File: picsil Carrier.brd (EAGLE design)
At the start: 95 x 54.3 mm, 52 parts, among them IC1 NAND, J1 STX-3120-3BM, J2 STX-3120-3BM, J3 STX-3120-3BM, J5 S2B-PH-SM4-TB(LF)(SN), J6 47346-1001, Q1 MMBT2222A, U1 MB85RC256VPF-G-JNERE2, U11 BORON, U2 TPL5010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

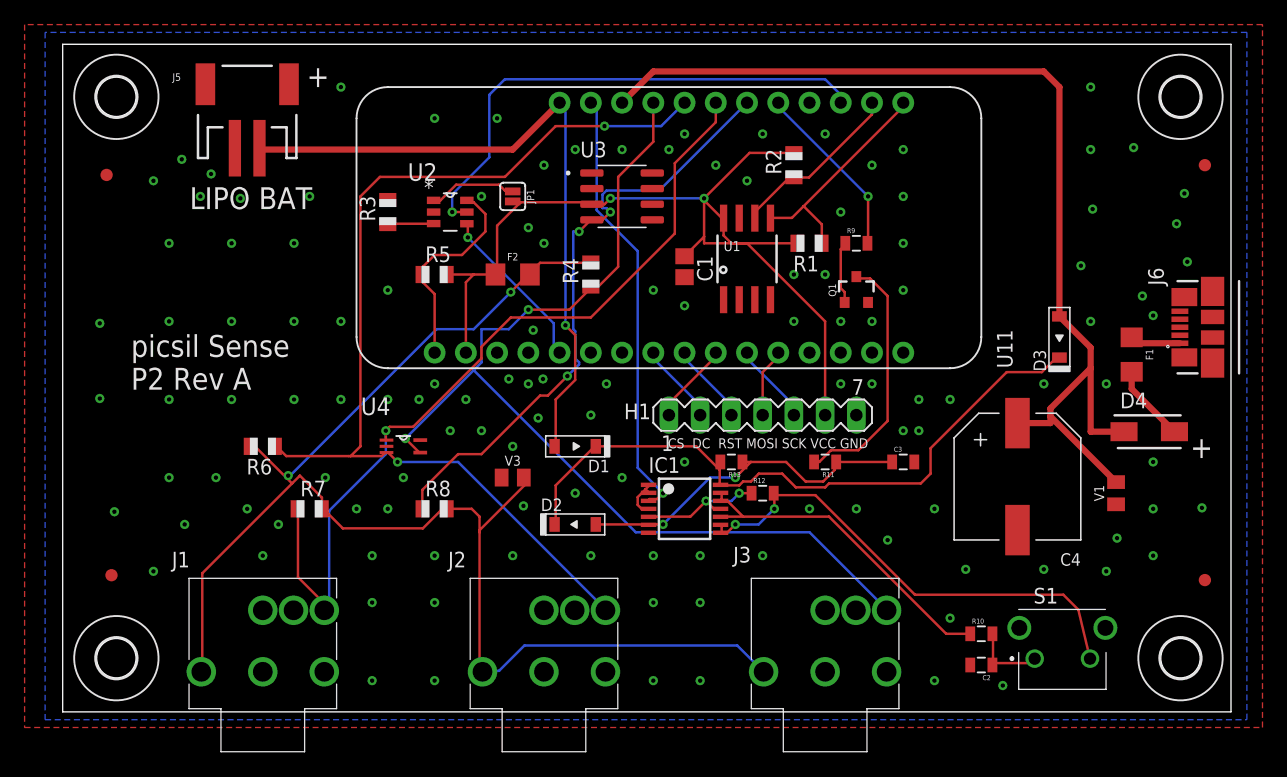
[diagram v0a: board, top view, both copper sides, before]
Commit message: rerouted VCC to U1
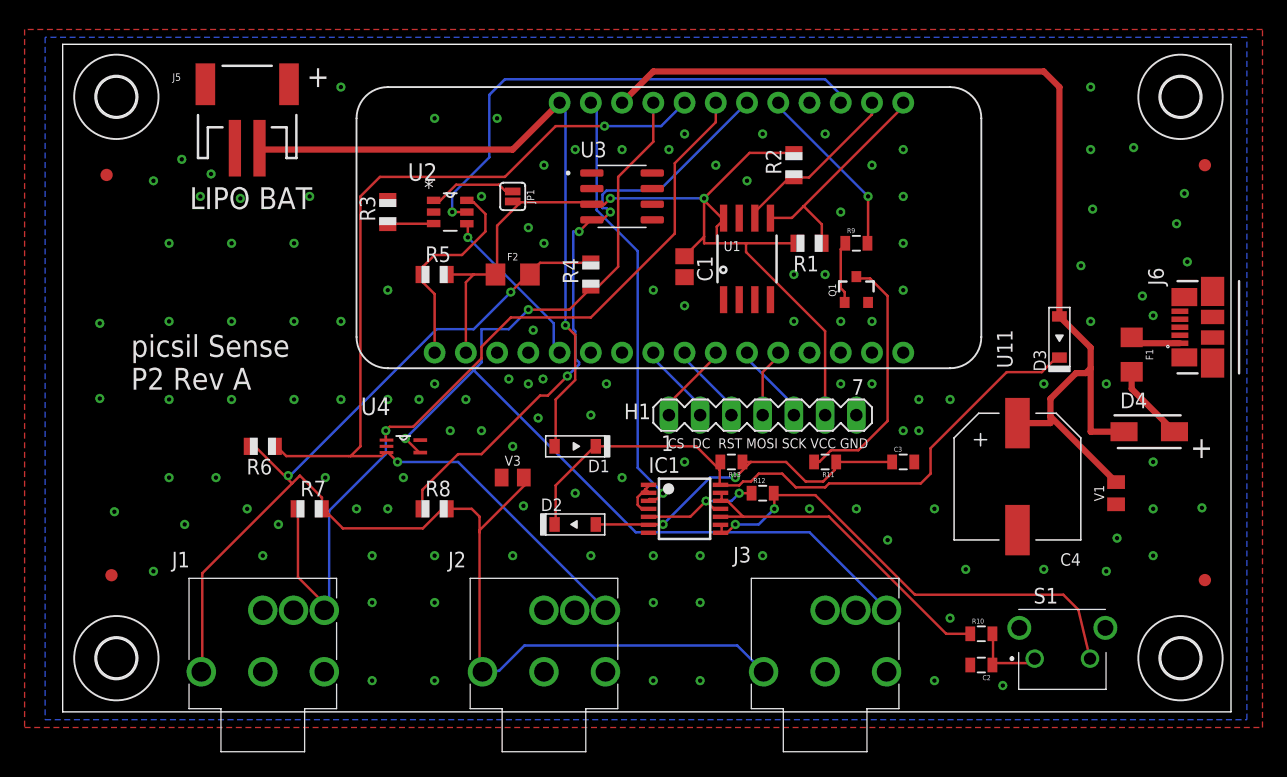
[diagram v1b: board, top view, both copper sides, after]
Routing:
- net VCC: track 78.1 -> 76.9 mm
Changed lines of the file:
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@@
 <vertex x="-5.000625" y="-0.635"/>
 <vertex x="92.71" y="-0.635"/>
-<vertex x="92.71" y="55.245"/>
-<vertex x="-5.000625" y="55.245"/>
+<vertex x="92.71" y="54.848125"/>
+<vertex x="-5.000625" y="54.848125"/>
 </polygon>
 <polygon width="0.1524" layer="1" isolate="0.3048">
 <vertex x="-6.6675" y="-1.27"/>
 <vertex x="93.98" y="-1.27"/>
-<vertex x="93.98" y="55.88"/>
-<vertex x="-6.6675" y="55.88"/>
+<vertex x="93.98" y="55.483125"/>
+<vertex x="-6.6675" y="55.483125"/>
 </polygon>
 <via x="52.07" y="43.18" extent="1-16" drill="0.35"/>
@@
 <wire x1="48.5775" y1="38.1" x2="48.5775" y2="38.6325" width="0.2032" layer="1"/>
 <wire x1="48.5775" y1="38.6325" x2="48.5775" y2="41.75125" width="0.2032" layer="1"/>
-<wire x1="48.5775" y1="38.1" x2="56.15" y2="38.1" width="0.2032" layer="1"/>
+<wire x1="48.5775" y1="38.1" x2="49.609375" y2="38.1" width="0.2032" layer="1"/>
+<wire x1="56.15" y1="38.1" x2="51.990625" y2="38.1" width="0.2032" layer="1"/>
+<wire x1="51.990625" y1="38.1" x2="49.609375" y2="38.1" width="0.2032" layer="1"/>
 <wire x1="31.62" y1="35.56" x2="29.845" y2="35.56" width="0.2032" layer="1"/>
 <wire x1="29.845" y1="35.56" x2="27.67" y2="35.56" width="0.2032" layer="1"/>
@@
 <wire x1="40.48125" y1="41.275" x2="40.9575" y2="41.75125" width="0.2032" layer="1"/>
 <wire x1="39.455" y1="41.275" x2="40.48125" y2="41.275" width="0.2032" layer="1"/>
-<wire x1="58.42" y1="31.75" x2="58.42" y2="24.13" width="0.2032" layer="1"/>
-<wire x1="52.07" y1="38.1" x2="58.42" y2="31.75" width="0.2032" layer="1"/>
-<wire x1="50.8" y1="38.1" x2="52.07" y2="38.1" width="0.2032" layer="1"/>
-<wire x1="50.165" y1="38.735" x2="50.8" y2="38.1" width="0.2032" layer="1"/>
-<wire x1="50.165" y1="40.005" x2="50.165" y2="38.735" width="0.2032" layer="1"/>
-<wire x1="50.165" y1="40.005" x2="50.165" y2="40.145" width="0.2032" layer="1"/>
+<wire x1="58.42" y1="24.13" x2="58.42" y2="30.95625" width="0.2032" layer="1"/>
 <via x="48.5775" y="41.75125" extent="1-16" drill="0.35"/>
 <via x="40.9575" y="41.75125" extent="1-16" drill="0.35"/>
@@
 <wire x1="29.21" y1="34.925" x2="29.845" y2="35.56" width="0.2032" layer="1"/>
 <wire x1="29.21" y1="29.21" x2="29.21" y2="34.925" width="0.2032" layer="1"/>
+<wire x1="49.609375" y1="39.449375" x2="50.165" y2="40.005" width="0.2032" layer="1"/>
+<wire x1="49.609375" y1="38.1" x2="49.609375" y2="39.449375" width="0.2032" layer="1"/>
+<wire x1="51.990625" y1="37.385625" x2="51.990625" y2="38.1" width="0.2032" layer="1"/>
+<wire x1="58.42" y1="30.95625" x2="51.990625" y2="37.385625" width="0.2032" layer="1"/>
+<wire x1="50.165" y1="40.145" x2="50.165" y2="40.005" width="0.2032" layer="1"/>
 </signal>
 <signal name="SDA">
@@
 <wire x1="80.01" y1="29.615" x2="80.01" y2="27.94" width="0.508" layer="1"/>
 <wire x1="80.01" y1="27.94" x2="80.01" y2="22.780625" width="0.508" layer="1"/>
-<wire x1="76.74" y1="24.67" x2="80.01" y2="27.94" width="0.508" layer="1"/>
+<wire x1="78.819375" y1="27.543125" x2="76.74" y2="25.46375" width="0.508" layer="1"/>
+<wire x1="78.819375" y1="27.543125" x2="79.613125" y2="27.543125" width="0.508" layer="1"/>
+<wire x1="79.613125" y1="27.543125" x2="80.01" y2="27.94" width="0.508" layer="1"/>
 <wire x1="77.47" y1="32.155" x2="77.47" y2="50.8" width="0.508" layer="1"/>
 <wire x1="77.47" y1="50.8" x2="76.2" y2="52.07" width="0.508" layer="1"/>
@@
 <wire x1="82.07375" y1="18.6817" x2="76.74" y2="24.01545" width="0.508" layer="1"/>
 <wire x1="76.74" y1="23.479375" x2="76.74" y2="24.01545" width="0.508" layer="1"/>
-<wire x1="76.74" y1="24.01545" x2="76.74" y2="24.67" width="0.508" layer="1"/>
+<wire x1="76.74" y1="24.01545" x2="76.74" y2="25.46375" width="0.508" layer="1"/>
 <wire x1="82.7225" y1="22.780625" x2="80.01" y2="22.780625" width="0.508" layer="1"/>
 <wire x1="44.45" y1="52.07" x2="41.91" y2="49.53" width="0.508" layer="1"/>
